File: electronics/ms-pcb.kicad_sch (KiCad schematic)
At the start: 27 parts, among them J1 Left motor, J2 Right motor, J3 XT60-M, U1 ESP32-S3-DEVKITC-1U-N8R2, U2 GY-521

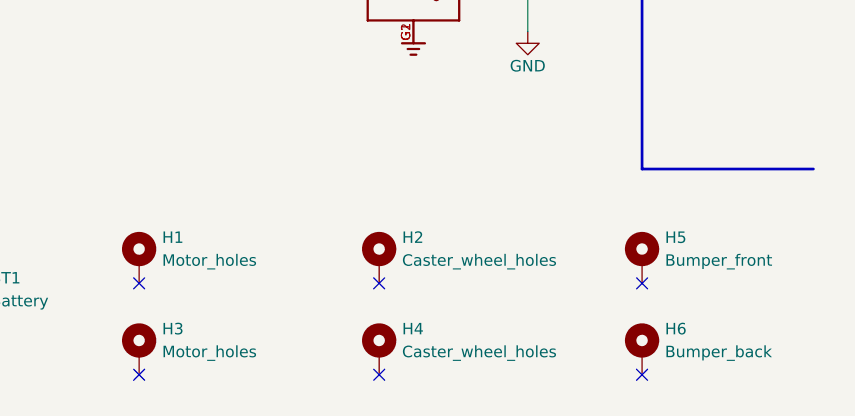
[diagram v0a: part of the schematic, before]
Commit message: fix: finish PCB layout v1.0.0
Closes: #10
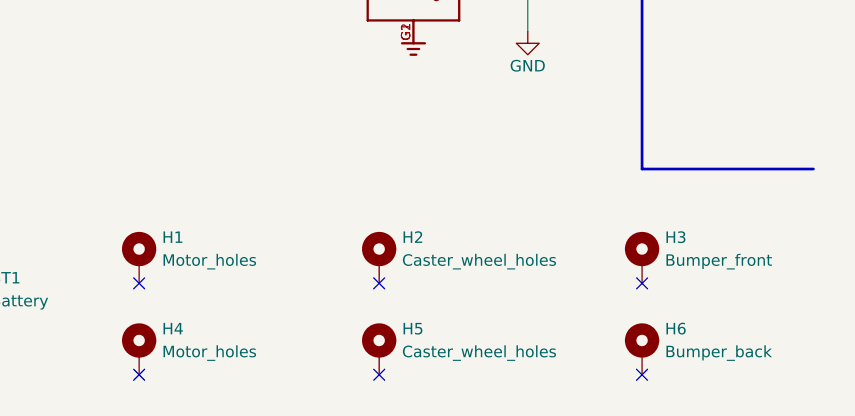
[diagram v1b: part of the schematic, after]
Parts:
- LS1: footprint footprints:SPKR_PKLCS1212E20A0-R1 -> footprints:buzzer_double_footprint
- renumbered H5 to H3, H3 to H4, H4 to H5
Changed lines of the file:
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@@
 		(on_board yes)
 		(dnp no)
-		(property "Reference" "#PWR030"
+		(property "Reference" "#PWR029"
 			(at 21.59 160.02 0)
 			(effects
@@
 			(project "ms-pcb"
 				(path "/5a2e0bf0-b2b3-43a5-bee5-ac51f9bc0574"
-					(reference "#PWR030")
+					(reference "#PWR029")
 					(unit 1)
 				)
@@
 		(dnp no)
 		(fields_autoplaced yes)
-		(property "Reference" "#PWR018"
+		(property "Reference" "#PWR019"
 			(at 227.33 125.73 0)
 			(effects
@@
 			(project "ms-pcb"
 				(path "/5a2e0bf0-b2b3-43a5-bee5-ac51f9bc0574"
-					(reference "#PWR018")
+					(reference "#PWR019")
 					(unit 1)
 				)
@@
 		(dnp no)
 		(fields_autoplaced yes)
-		(property "Reference" "#PWR033"
+		(property "Reference" "#PWR032"
 			(at 21.59 191.77 0)
 			(effects
@@
 			(project "ms-pcb"
 				(path "/5a2e0bf0-b2b3-43a5-bee5-ac51f9bc0574"
-					(reference "#PWR033")
+					(reference "#PWR032")
 					(unit 1)
 				)
@@
 		(on_board yes)
 		(dnp no)
-		(property "Reference" "#PWR032"
+		(property "Reference" "#PWR031"
 			(at 57.15 160.02 0)
 			(effects
@@
 			(project "ms-pcb"
 				(path "/5a2e0bf0-b2b3-43a5-bee5-ac51f9bc0574"
-					(reference "#PWR032")
+					(reference "#PWR031")
 					(unit 1)
 				)
@@
 		(on_board yes)
 		(dnp no)
-		(property "Reference" "#PWR029"
+		(property "Reference" "#PWR028"
 			(at 144.78 157.48 0)
 			(effects
@@
 			(project "ms-pcb"
 				(path "/5a2e0bf0-b2b3-43a5-bee5-ac51f9bc0574"
-					(reference "#PWR029")
+					(reference "#PWR028")
 					(unit 1)
 				)
@@
 		(dnp no)
 		(fields_autoplaced yes)
-		(property "Reference" "H4"
+		(property "Reference" "H5"
 			(at 130.81 184.1499 0)
 			(effects
@@
 			(project "ms-pcb"
 				(path "/5a2e0bf0-b2b3-43a5-bee5-ac51f9bc0574"
-					(reference "H4")
+					(reference "H5")
 					(unit 1)
 				)
@@
 		(on_board yes)
 		(dnp no)
-		(property "Reference" "#PWR019"
+		(property "Reference" "#PWR020"
 			(at 172.72 129.54 0)
 			(effects
@@
 			(project "ms-pcb"
 				(path "/5a2e0bf0-b2b3-43a5-bee5-ac51f9bc0574"
-					(reference "#PWR019")
+					(reference "#PWR020")
 					(unit 1)
 				)
@@
 		(dnp no)
 		(fields_autoplaced yes)
-		(property "Reference" "H5"
+		(property "Reference" "H3"
 			(at 160.02 173.9899 0)
 			(effects
@@
 			(project "ms-pcb"
 				(path "/5a2e0bf0-b2b3-43a5-bee5-ac51f9bc0574"
-					(reference "H5")
+					(reference "H3")
 					(unit 1)
 				)
@@
 		(dnp no)
 		(fields_autoplaced yes)
-		(property "Reference" "#PWR020"
+		(property "Reference" "#PWR018"
 			(at 115.57 121.92 0)
 			(effects
@@
 			(project "ms-pcb"
 				(path "/5a2e0bf0-b2b3-43a5-bee5-ac51f9bc0574"
-					(reference "#PWR020")
+					(reference "#PWR018")
 					(unit 1)
 				)
@@
 		(on_board yes)
 		(dnp no)
-		(property "Reference" "#PWR028"
+		(property "Reference" "#PWR027"
 			(at 204.47 153.67 0)
 			(effects
@@
 			(project "ms-pcb"
 				(path "/5a2e0bf0-b2b3-43a5-bee5-ac51f9bc0574"
-					(reference "#PWR028")
+					(reference "#PWR027")
 					(unit 1)
 				)
@@
 		(dnp no)
 		(fields_autoplaced yes)
-		(property "Reference" "#PWR0101"
+		(property "Reference" "#PWR030"
 			(at 39.37 160.02 0)
 			(effects
@@
 			(project "ms-pcb"
 				(path "/5a2e0bf0-b2b3-43a5-bee5-ac51f9bc0574"
-					(reference "#PWR0101")
+					(reference "#PWR030")
 					(unit 1)
 				)
@@
 		(dnp no)
 		(fields_autoplaced yes)
-		(property "Reference" "#PWR035"
+		(property "Reference" "#PWR034"
 			(at 57.15 191.77 0)
 			(effects
@@
 			(project "ms-pcb"
 				(path "/5a2e0bf0-b2b3-43a5-bee5-ac51f9bc0574"
-					(reference "#PWR035")
+					(reference "#PWR034")
 					(unit 1)
 				)
@@
 			)
 		)
-		(property "Footprint" "footprints:SPKR_PKLCS1212E20A0-R1"
+		(property "Footprint" "footprints:buzzer_double_footprint"
 			(at 81.28 134.62 0)
 			(effects
@@
 		(dnp no)
 		(fields_autoplaced yes)
-		(property "Reference" "H3"
+		(property "Reference" "H4"
 			(at 104.14 184.1499 0)
 			(effects
@@
 			(project "ms-pcb"
 				(path "/5a2e0bf0-b2b3-43a5-bee5-ac51f9bc0574"
-					(reference "H3")
+					(reference "H4")
 					(unit 1)
 				)
@@
 		(dnp no)
 		(fields_autoplaced yes)
-		(property "Reference" "#PWR034"
+		(property "Reference" "#PWR033"
 			(at 39.37 191.77 0)
 			(effects
@@
 			(project "ms-pcb"
 				(path "/5a2e0bf0-b2b3-43a5-bee5-ac51f9bc0574"
-					(reference "#PWR034")
+					(reference "#PWR033")
 					(unit 1)
 				)

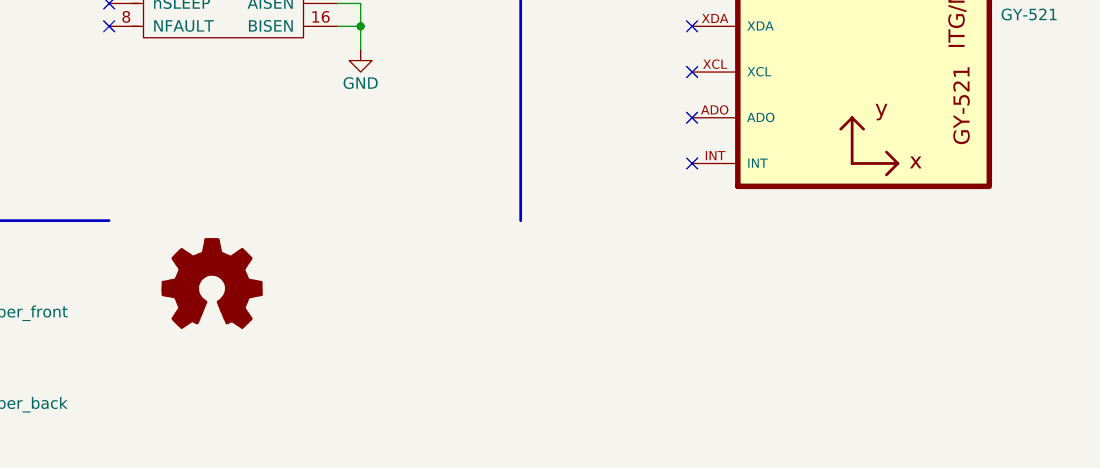
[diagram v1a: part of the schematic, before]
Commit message: elec: export schematic of pcb v1.0.0 as pdf
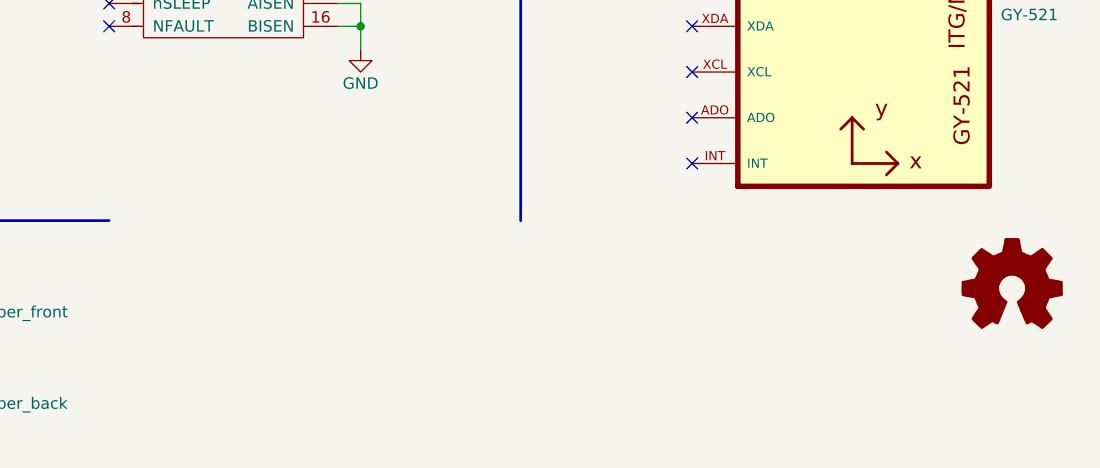
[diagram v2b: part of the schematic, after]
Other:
- company: (none) -> OTH Regensburg / HEIG-VD
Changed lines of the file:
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@@
 	(title_block
 		(title "Algernon Micromouse PCB")
-		(rev "v0.1")
+		(date "2024-04-24")
+		(rev "v1.0.0")
+		(company "OTH Regensburg / HEIG-VD")
 	)
 	(junction
@@
 	(symbol
 		(lib_id "Graphic:Logo_Open_Hardware_Small")
-		(at 187.96 173.99 0)
+		(at 276.86 173.99 0)
 		(unit 1)
 		(exclude_from_sim no)
@@
 		(fields_autoplaced yes)
 		(property "Reference" "#LOGO1"
-			(at 187.96 167.005 0)
+			(at 276.86 167.005 0)
 			(effects
 				(font
@@
 		)
 		(property "Value" "Logo_Open_Hardware_Small"
-			(at 187.96 179.705 0)
+			(at 276.86 179.705 0)
 			(effects
 				(font
@@
 		)
 		(property "Footprint" ""
-			(at 187.96 173.99 0)
+			(at 276.86 173.99 0)
 			(effects
 				(font
@@
 		)
 		(property "Datasheet" "~"
-			(at 187.96 173.99 0)
+			(at 276.86 173.99 0)
 			(effects
 				(font
@@
 		)
 		(property "Description" ""
-			(at 187.96 173.99 0)
+			(at 276.86 173.99 0)
 			(effects
 				(font

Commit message: elec: start PCB v1.1.0
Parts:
- added C1, C2: 0.1uF, Capacitor_THT:CP_Radial_D5.0mm_P2.00mm, symbol Device:C
- added D1: D_Schottky, Diode_SMD:D_1206_3216Metric_Pad1.42x1.75mm_HandSolder, symbol Device:D_Schottky
- added D2: DEBUG, LED_SMD:LED_1206_3216Metric_Pad1.42x1.75mm_HandSolder, symbol Device:LED
- added R3: 10k, Resistor_SMD:R_1206_3216Metric_Pad1.30x1.75mm_HandSolder, symbol Device:R
- added R4: 5k, Resistor_SMD:R_1206_3216Metric_Pad1.30x1.75mm_HandSolder, symbol Device:R
- added R8: 1k, Resistor_SMD:R_1206_3216Metric_Pad1.30x1.75mm_HandSolder, symbol Device:R
- H5: renamed from H2; value Caster_wheel_holes -> Caster_wheel
- H6: renamed from H5; value Caster_wheel_holes -> Caster_wheel
- J3: Description_1 (none) -> Plug; DC supply; XT60; male; PIN: 2; for cable; soldered; 3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
- R5: renamed from R3; value 220 -> 40k
- R6: renamed from R4; value 220 -> 5k
- U1: Description_1 (none) -> WiFi Development Tools - 802.11 ESP32-S3 Gen-Purpose Dev Bd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
- U2: Description_1 (none) -> Triple Axis Accelerometer Gyro Breakout
- renumbered D1 to D3, D2 to D4, H3 to H1, H6 to H2, H1 to H3, R5 to R7
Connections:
- net +3.3V: now also R3.1
- net +BATT: now also D1.2 (A); no longer U1.J1_21 (5V0)
- net DRV_L1: now also U1.J1_14 (GPIO46); no longer U1.J3_13 (GPIO35)
- net DRV_L2: now also U1.J1_15 (GPIO9); no longer U1.J3_12 (GPIO36)
- net DRV_R1: now also U1.J1_17 (GPIO11); no longer U1.J3_10 (GPIO38)
- net DRV_R2: now also U1.J1_16 (GPIO10); no longer U1.J3_11 (GPIO37)
- net ENC_L1: now also U1.J1_4 (GPIO4); no longer U1.J3_20 (USB_D-/GPIO19)
- net ENC_L2: now also U1.J1_5 (GPIO5); no longer U1.J3_18 (GPIO21)
- net ENC_R1: now also U1.J1_19 (GPIO13); no longer U1.J3_7 (MTDI/GPIO41)
- net ENC_R2: now also U1.J1_20 (GPIO14); no longer U1.J3_6 (MTMS/GPIO42)
- net GND: now also D2.1 (K), R8.2
- net MOT_L1: now also C1.2
- net MOT_L2: now also C1.1
- net MOT_R1: now also C2.2
- net MOT_R2: now also C2.1
- net SCL: now also U1.J3_18 (GPIO21); no longer U1.J1_5 (GPIO5)
- net SDA: now also U1.J3_17 (GPIO47); no longer U1.J1_4 (GPIO4)
- net XSHUT_FL: now also U1.J3_4 (GPIO1); no longer U1.J1_20 (GPIO14)
- net XSHUT_FR: now also U1.J3_19 (USB_D+/GPIO20); no longer U1.J1_16 (GPIO10)
- net XSHUT_L: now also U1.J3_8 (MTDO/GPIO40); no longer U1.J1_19 (GPIO13)
- net XSHUT_R: now also U1.J3_20 (USB_D-/GPIO19); no longer U1.J1_17 (GPIO11)
- net button: now also U1.J1_10 (GPIO17); no longer U1.J3_17 (GPIO47)
- net buzzer: now also U1.J1_6 (GPIO6); no longer U1.J3_16 (GPIO48)
- net Mes_bat: now reaches U1.J1_13 (GPIO3)
- net Mes_bat: now also R2.2, R7.1
- net DEBUG: now reaches U1.J3_5 (GPIO2)
- net DEBUG: now also R4.1
- removed net Vmes: R2.2, R7.1, U1.J3_19 (USB_D+/GPIO20)
- new net: D2.2 (A), R4.2
- new net: D1.1 (K), U1.J1_21 (5V0)
- new net Mes_VCC: R3.2, R8.1, U1.J3_16 (GPIO48)
- no-connect marks 22 -> 40
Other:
- moved on the sheet: BT1, D3, D4, H1, H2, H3, H4, H5, H6, J1, J2, J3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

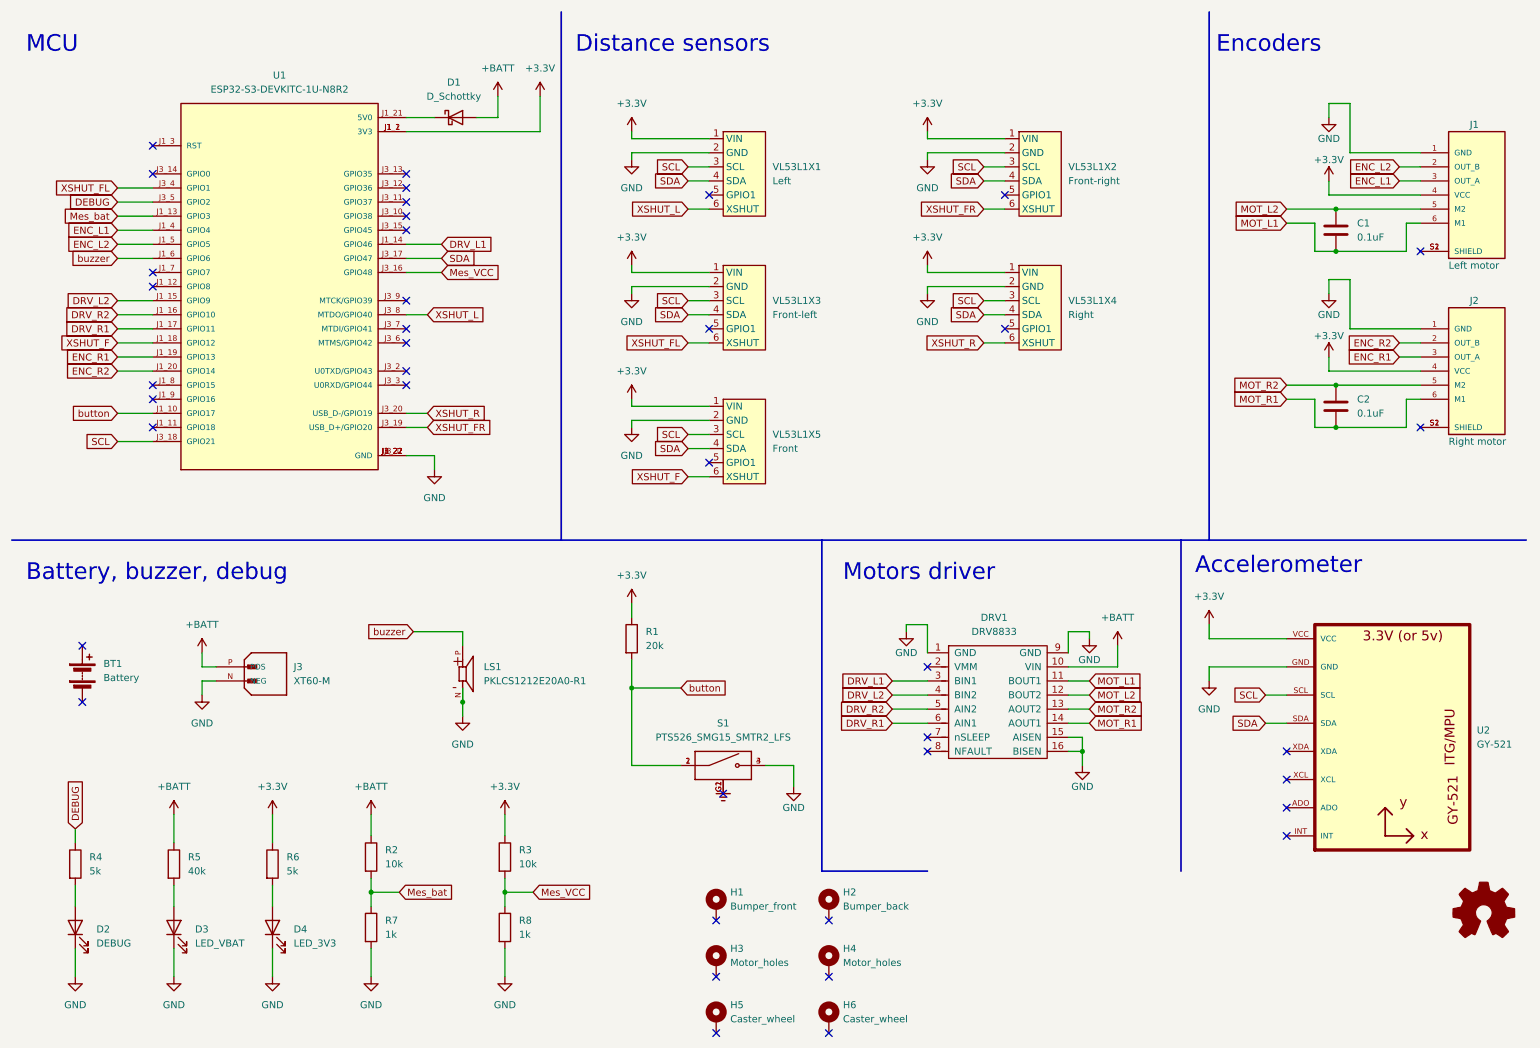
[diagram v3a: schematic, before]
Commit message: elec: PCB v1.1.0 finished
Still need last checks before ordering.
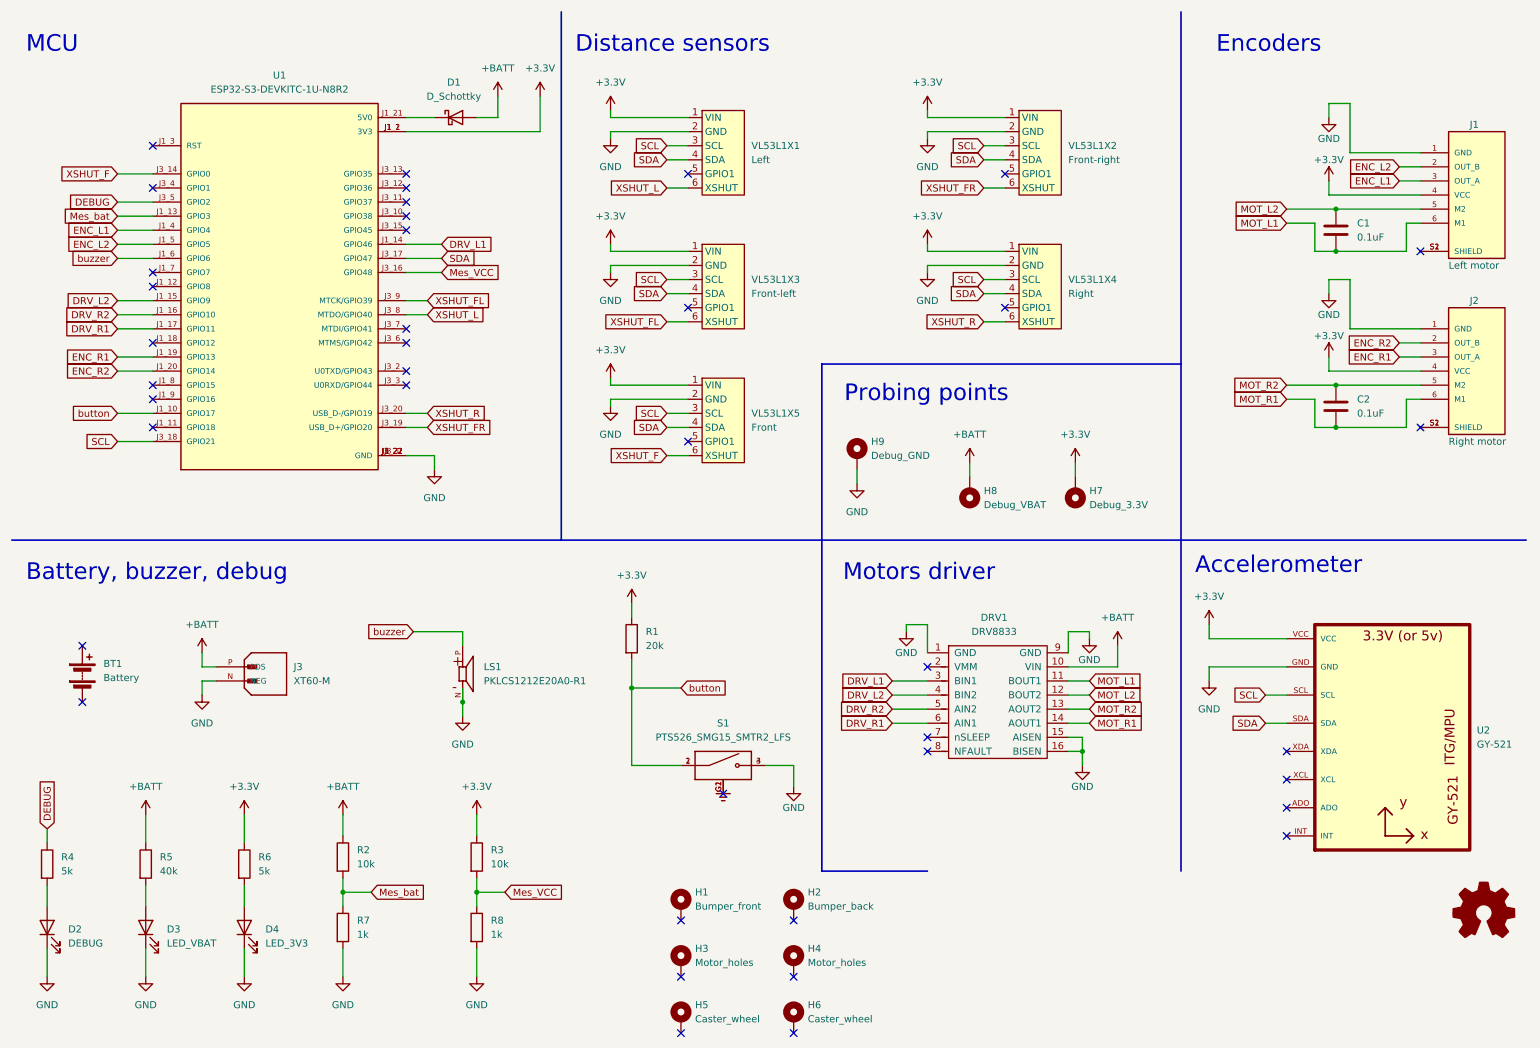
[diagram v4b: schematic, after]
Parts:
- added H7: Debug_3.3V, Connector_Wire:SolderWire-0.75sqmm_1x01_D1.25mm_OD2.3mm, symbol Mechanical:MountingHole_Pad
- added H8: Debug_VBAT, Connector_Wire:SolderWire-0.75sqmm_1x01_D1.25mm_OD2.3mm, symbol Mechanical:MountingHole_Pad
- added H9: Debug_GND, Connector_Wire:SolderWire-0.75sqmm_1x01_D1.25mm_OD2.3mm, symbol Mechanical:MountingHole_Pad
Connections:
- net +3.3V: now also H7.1
- net +BATT: now also H8.1
- net GND: now also H9.1
- net XSHUT_F: now also U1.J3_14 (GPIO0); no longer U1.J1_18 (GPIO12)
- net XSHUT_FL: now also U1.J3_9 (MTCK/GPIO39); no longer U1.J3_4 (GPIO1)
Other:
- note added: "Probing points"
- moved on the sheet: D2, D3, D4, H1, H2, H3, H4, H5, H6, R2, R3, R4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

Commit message: elec: final check for PCB v1.1.0
Refs: #51
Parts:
- added C3: 220uF, Capacitor_SMD:CP_Elec_8x10.5, symbol Device:C
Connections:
- net +BATT: now also C3.1
- net GND: now also C3.2
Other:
- moved on the sheet: BT1, J3

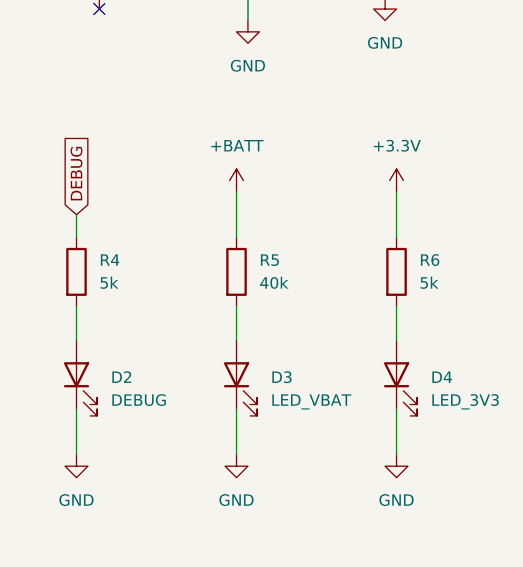
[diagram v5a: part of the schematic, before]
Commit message: docs: fix v1.1.0 pin mapping
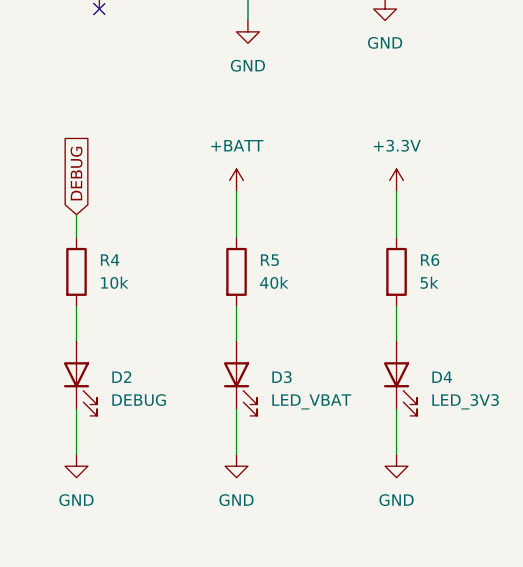
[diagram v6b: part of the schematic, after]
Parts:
- R4: value 5k -> 10k
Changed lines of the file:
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@@
 			)
 		)
-		(property "Value" "5k"
+		(property "Value" "10k"
 			(at 20.32 166.3699 0)
 			(effects
